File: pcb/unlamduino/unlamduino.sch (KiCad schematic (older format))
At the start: 37 parts, among them IC2 ATMEGA328-P, P3 CONN_01X08, U1 LM2576, U2 AP111733, Y2 16MHz

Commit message: Primera asignacion de encapsulados a las partes del circuito.
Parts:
- AD1: footprint (none) -> Pin_Headers:Pin_Header_Straight_1x06
- C1, C3: footprint (none) -> Capacitors_ThroughHole:C_Radial_D6.3_L11.2_P2.5
- C10, C2, C4, C5, C6, C7, C9: footprint (none) -> Capacitors_ThroughHole:C_Disc_D6_P5
- C20, C21: footprint (none) -> Capacitors_ThroughHole:C_Disc_D3_P2.5
- C8: footprint (none) -> Capacitors_ThroughHole:C_Radial_D7.5_L11.2_P2.5
- D2, D5, D6: footprint (none) -> Diodes_ThroughHole:Diode_DO-41_SOD81_Horizontal_RM10
- D4, DR1: footprint (none) -> LEDs:LED-5MM
- ICSP2: footprint (none) -> Pin_Headers:Pin_Header_Straight_2x03
- IOH1: footprint (none) -> Pin_Headers:Pin_Header_Straight_1x10
- IOL1, P3: footprint (none) -> Pin_Headers:Pin_Header_Straight_1x08
- JP1: footprint (none) -> Connect:BARREL_JACK
- L2: footprint (none) -> Resistors_ThroughHole:Resistor_Horizontal_RM10mm
- L3: footprint (none) -> Discret:CP36V
- PSerial1: footprint (none) -> Pin_Headers:Pin_Header_Straight_1x04
- PWR1: footprint (none) -> Connect:bornier2
- R1, R8, R9, RN1, RN2: footprint (none) -> Resistors_ThroughHole:Resistor_Horizontal_RM15mm
- RESET1: footprint (none) -> Buttons_Switches_ThroughHole:SW_PUSH_SMALL
- U1: footprint (none) -> TO_SOT_Packages_THT:Pentawatt_Neutral_Staggered_Verical_TO220-5-T05D
- Y2: footprint (none) -> Crystals:Crystal_HC51-U_Vertical
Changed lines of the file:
@@
 F 0 "IOL1" H 7400 5950 50  0000 C CNN
 F 1 "CONN_01X08" V 7500 5500 50  0001 C CNN
-F 2 "" H 7400 5500 60  0000 C CNN
+F 2 "Pin_Headers:Pin_Header_Straight_1x08" H 7400 5500 60  0001 C CNN
 F 3 "" H 7400 5500 60  0000 C CNN
 	1    7400 5500
@@
 F 0 "IOH1" H 8850 4550 50  0000 C CNN
 F 1 "CONN_01X10" V 8950 4000 50  0001 C CNN
-F 2 "" H 8850 4000 60  0000 C CNN
+F 2 "Pin_Headers:Pin_Header_Straight_1x10" H 8850 4000 60  0001 C CNN
 F 3 "" H 8850 4000 60  0000 C CNN
 	1    8850 4000
@@
 F 0 "ICSP2" H 10100 4850 50  0000 C CNN
 F 1 "CONN_02X03" H 10100 4450 50  0000 C CNN
-F 2 "" H 10100 3450 60  0000 C CNN
+F 2 "Pin_Headers:Pin_Header_Straight_2x03" H 10100 3450 60  0001 C CNN
 F 3 "" H 10100 3450 60  0000 C CNN
 	1    10100 4650
@@
 F 0 "C10" H 2750 4700 50  0000 L CNN
 F 1 "100nF" H 2750 4600 50  0000 L CNN
-F 2 "" H 2600 4600 60  0000 C CNN
+F 2 "Capacitors_ThroughHole:C_Disc_D6_P5" H 2600 4600 60  0001 C CNN
 F 3 "" H 2600 4600 60  0000 C CNN
 	1    2600 4600
@@
 F 0 "D4" H 7150 2650 50  0000 L CNN
 F 1 "Verde" H 7050 2470 50  0000 L CNN
-F 2 "" V 7200 2550 60  0000 C CNN
+F 2 "LEDs:LED-5MM" V 7200 2550 60  0001 C CNN
 F 3 "" V 7200 2550 60  0000 C CNN
 	1    7200 2550
@@
 F 0 "R8" V 4750 6400 50  0000 C CNN
 F 1 "1K" V 4850 6400 50  0000 C CNN
-F 2 "" V 4780 6400 50  0000 C CNN
+F 2 "Resistors_ThroughHole:Resistor_Horizontal_RM15mm" V 4780 6400 50  0001 C CNN
 F 3 "" H 4850 6400 50  0000 C CNN
 	1    4850 6400
@@
 F 0 "R9" V 4930 6500 50  0000 C CNN
 F 1 "1K" V 4850 6500 50  0000 C CNN
-F 2 "" V 4780 6500 50  0000 C CNN
+F 2 "Resistors_ThroughHole:Resistor_Horizontal_RM15mm" V 4780 6500 50  0001 C CNN
 F 3 "" H 4850 6500 50  0000 C CNN
 	1    4850 6500
@@
 F 0 "C7" H 2275 4100 50  0000 L CNN
 F 1 "100nF" H 2275 3900 50  0000 L CNN
-F 2 "" H 2288 3850 50  0000 C CNN
+F 2 "Capacitors_ThroughHole:C_Disc_D6_P5" H 2288 3850 50  0001 C CNN
 F 3 "" H 2250 4000 50  0000 C CNN
 	1    2250 4000
@@
 F 0 "C5" H 1975 4100 50  0000 L CNN
 F 1 "100nF" H 1975 3900 50  0000 L CNN
-F 2 "" H 1988 3850 50  0000 C CNN
+F 2 "Capacitors_ThroughHole:C_Disc_D6_P5" H 1988 3850 50  0001 C CNN
 F 3 "" H 1950 4000 50  0000 C CNN
 	1    1950 4000
@@
 F 0 "L2" V 2200 3900 50  0000 L CNN
 F 1 "L_Small" V 2200 3550 50  0000 L CNN
-F 2 "" H 2100 3850 50  0000 C CNN
+F 2 "Resistors_ThroughHole:Resistor_Horizontal_RM10mm" H 2100 3850 50  0001 C CNN
 F 3 "" H 2100 3850 50  0000 C CNN
 	1    2100 3850
@@
 F 0 "Y2" V 9550 5800 50  0000 C CNN
 F 1 "16MHz" V 9650 5800 50  0000 C CNN
-F 2 "" H 9850 5800 50  0000 C CNN
+F 2 "Crystals:Crystal_HC51-U_Vertical" H 9850 5800 50  0001 C CNN
 F 3 "" H 9850 5800 50  0000 C CNN
 	1    9850 5800
@@
 F 0 "C20" V 9950 5600 50  0000 L CNN
 F 1 "22pF" V 9850 5600 50  0000 L CNN
-F 2 "" H 10188 5500 50  0000 C CNN
+F 2 "Capacitors_ThroughHole:C_Disc_D3_P2.5" H 10188 5500 50  0001 C CNN
 F 3 "" H 10150 5650 50  0000 C CNN
 	1    10150 5650
@@
 F 0 "C21" V 10300 5900 50  0000 L CNN
 F 1 "22pF" V 10400 5900 50  0000 L CNN
-F 2 "" H 10188 5800 50  0000 C CNN
+F 2 "Capacitors_ThroughHole:C_Disc_D3_P2.5" H 10188 5800 50  0001 C CNN
 F 3 "" H 10150 5950 50  0000 C CNN
 	1    10150 5950
@@
 F 0 "RN1" V 1450 5800 50  0000 C CNN
 F 1 "10K" V 1550 5800 50  0000 C CNN
-F 2 "" V 1480 5800 50  0000 C CNN
+F 2 "Resistors_ThroughHole:Resistor_Horizontal_RM15mm" V 1480 5800 50  0001 C CNN
 F 3 "" H 1550 5800 50  0000 C CNN
 	1    1550 5800
@@
 F 0 "C6" H 1300 6550 50  0000 L CNN
 F 1 "100nF" H 1300 6650 50  0000 L CNN
-F 2 "" H 1588 6400 50  0000 C CNN
+F 2 "Capacitors_ThroughHole:C_Disc_D6_P5" H 1588 6400 50  0001 C CNN
 F 3 "" H 1550 6550 50  0000 C CNN
 	1    1550 6550
@@
 F 0 "RESET1" H 1950 6660 50  0000 C CNN
 F 1 "SW_PUSH" H 1800 6470 50  0000 C CNN
-F 2 "" H 1800 6550 50  0000 C CNN
+F 2 "Buttons_Switches_ThroughHole:SW_PUSH_SMALL" H 1800 6550 50  0001 C CNN
 F 3 "" H 1800 6550 50  0000 C CNN
 	1    1800 6550
@@
 F 0 "P3" H 10400 4000 50  0000 C CNN
 F 1 "CONN_01X08" V 10500 3450 50  0000 C CNN
-F 2 "" H 10400 3450 50  0000 C CNN
+F 2 "Pin_Headers:Pin_Header_Straight_1x08" H 10400 3450 50  0001 C CNN
 F 3 "" H 10400 3450 50  0000 C CNN
 	1    10400 3450
@@
 F 0 "D5" H 3250 2000 50  0000 C CNN
 F 1 "1N4007" H 3250 1800 50  0000 C CNN
-F 2 "" H 3250 1900 50  0000 C CNN
+F 2 "Diodes_ThroughHole:Diode_DO-41_SOD81_Horizontal_RM10" H 3250 1900 50  0001 C CNN
 F 3 "" H 3250 1900 50  0000 C CNN
 	1    3250 1900
@@
 F 0 "C2" H 3875 2400 50  0000 L CNN
 F 1 "100nF" H 3875 2200 50  0000 L CNN
-F 2 "" H 3888 2150 50  0000 C CNN
+F 2 "Capacitors_ThroughHole:C_Disc_D6_P5" H 3888 2150 50  0001 C CNN
 F 3 "" H 3850 2300 50  0000 C CNN
 	1    3850 2300
@@
 F 0 "C1" H 3575 2400 50  0000 L CNN
 F 1 "100uF 35V" H 3100 2150 50  0000 L CNN
-F 2 "" H 3550 2300 50  0000 C CNN
+F 2 "Capacitors_ThroughHole:C_Radial_D6.3_L11.2_P2.5" H 3550 2300 50  0001 C CNN
 F 3 "" H 3550 2300 50  0000 C CNN
 	1    3550 2300
@@
 F 0 "C4" H 6825 2400 50  0000 L CNN
 F 1 "100nF" H 6850 2200 50  0000 L CNN
-F 2 "" H 6838 2150 50  0000 C CNN
+F 2 "Capacitors_ThroughHole:C_Disc_D6_P5" H 6838 2150 50  0001 C CNN
 F 3 "" H 6800 2300 50  0000 C CNN
 	1    6800 2300
@@
 F 0 "C3" H 6525 2400 50  0000 L CNN
 F 1 "100uF 16v" H 6250 2150 50  0000 L CNN
-F 2 "" H 6500 2300 50  0000 C CNN
+F 2 "Capacitors_ThroughHole:C_Radial_D6.3_L11.2_P2.5" H 6500 2300 50  0001 C CNN
 F 3 "" H 6500 2300 50  0000 C CNN
 	1    6500 2300
@@
 F 0 "D6" H 5800 2400 50  0000 C CNN
 F 1 "1N5819" H 5800 2200 50  0000 C CNN
-F 2 "" H 5800 2300 50  0000 C CNN
+F 2 "Diodes_ThroughHole:Diode_DO-41_SOD81_Horizontal_RM10" H 5800 2300 50  0001 C CNN
 F 3 "" H 5800 2300 50  0000 C CNN
 	1    5800 2300
@@
 F 0 "L3" V 6000 1950 50  0000 L CNN
 F 1 "330uHy" V 5900 1850 50  0000 L CNN
-F 2 "" H 6050 2000 50  0000 C CNN
+F 2 "Discret:CP36V" H 6050 2000 50  0001 C CNN
 F 3 "" H 6050 2000 50  0000 C CNN
 	1    6050 2000
@@
 F 0 "U1" H 4300 2350 50  0000 C CNN
 F 1 "LM2576" H 4400 2250 50  0000 C CNN
-F 2 "" H 4800 1950 79  0001 C CNN
+F 2 "TO_SOT_Packages_THT:Pentawatt_Neutral_Staggered_Verical_TO220-5-T05D" H 4800 1950 79  0001 C CNN
 F 3 "" H 4800 1950 79  0001 C CNN
 	1    4800 1950
@@
 F 0 "R1" H 7100 2050 50  0000 C CNN
 F 1 "470" V 7200 2200 50  0000 C CNN
-F 2 "" V 7130 2200 50  0000 C CNN
+F 2 "Resistors_ThroughHole:Resistor_Horizontal_RM15mm" V 7130 2200 50  0001 C CNN
 F 3 "" H 7200 2200 50  0000 C CNN
 	1    7200 2200
@@
 F 0 "D2" H 1800 5950 50  0000 C CNN
 F 1 "1N4007" H 1800 5750 50  0000 C CNN
-F 2 "" H 1800 5850 50  0000 C CNN
+F 2 "Diodes_ThroughHole:Diode_DO-41_SOD81_Horizontal_RM10" H 1800 5850 50  0001 C CNN
 F 3 "" H 1800 5850 50  0000 C CNN
 	1    1800 5850
@@
 F 0 "AD1" H 7400 5000 50  0000 C CNN
 F 1 "CONN_01X06" V 7500 4650 50  0001 C CNN
-F 2 "" H 7400 4650 60  0000 C CNN
+F 2 "Pin_Headers:Pin_Header_Straight_1x06" H 7400 4650 60  0001 C CNN
 F 3 "" H 7400 4650 60  0000 C CNN
 	1    7400 4650
@@
 F 0 "RN2" H 7750 4200 50  0000 C CNN
 F 1 "1K" V 7850 4350 50  0000 C CNN
-F 2 "" V 7780 4350 50  0000 C CNN
+F 2 "Resistors_ThroughHole:Resistor_Horizontal_RM15mm" V 7780 4350 50  0001 C CNN
 F 3 "" H 7850 4350 50  0000 C CNN
 	1    7850 4350
@@
 F 0 "DR1" H 7800 4800 50  0000 L CNN
 F 1 "Rojo" H 7700 4620 50  0000 L CNN
-F 2 "" V 7850 4700 60  0000 C CNN
+F 2 "LEDs:LED-5MM" V 7850 4700 60  0001 C CNN
 F 3 "" V 7850 4700 60  0000 C CNN
 	1    7850 4700
@@
 F 0 "PWR1" H 1800 2100 50  0000 C CNN
 F 1 "CONN_01X02" V 1900 1950 50  0001 C CNN
-F 2 "" H 1800 1950 50  0000 C CNN
+F 2 "Connect:bornier2" H 1800 1950 50  0001 C CNN
 F 3 "" H 1800 1950 50  0000 C CNN
 	1    1800 1950
@@
 F 0 "PSerial1" H 3950 6700 50  0000 C CNN
 F 1 "CONN_01X04" V 4050 6450 50  0001 C CNN
-F 2 "" H 3950 6450 50  0000 C CNN
+F 2 "Pin_Headers:Pin_Header_Straight_1x04" H 3950 6450 50  0001 C CNN
 F 3 "" H 3950 6450 50  0000 C CNN
 	1    3950 6450
@@
 F 0 "JP1" H 1700 1250 50  0000 C CNN
 F 1 "JACK_2P" H 1900 1700 50  0000 C CNN
-F 2 "" H 2050 1450 50  0000 C CNN
+F 2 "Connect:BARREL_JACK" H 2050 1450 50  0001 C CNN
 F 3 "" H 2050 1450 50  0000 C CNN
 	1    2050 1450
@@
 F 0 "C9" H 8375 2400 50  0000 L CNN
 F 1 "100nF" H 8400 2200 50  0000 L CNN
-F 2 "" H 8388 2150 50  0000 C CNN
+F 2 "Capacitors_ThroughHole:C_Disc_D6_P5" H 8388 2150 50  0001 C CNN
 F 3 "" H 8350 2300 50  0000 C CNN
 	1    8350 2300
@@
 F 0 "C8" H 8075 2400 50  0000 L CNN
 F 1 "100uF 16v" H 7800 2150 50  0000 L CNN
-F 2 "" H 8050 2300 50  0000 C CNN
+F 2 "Capacitors_ThroughHole:C_Radial_D7.5_L11.2_P2.5" H 8050 2300 50  0001 C CNN
 F 3 "" H 8050 2300 50  0000 C CNN
 	1    8050 2300

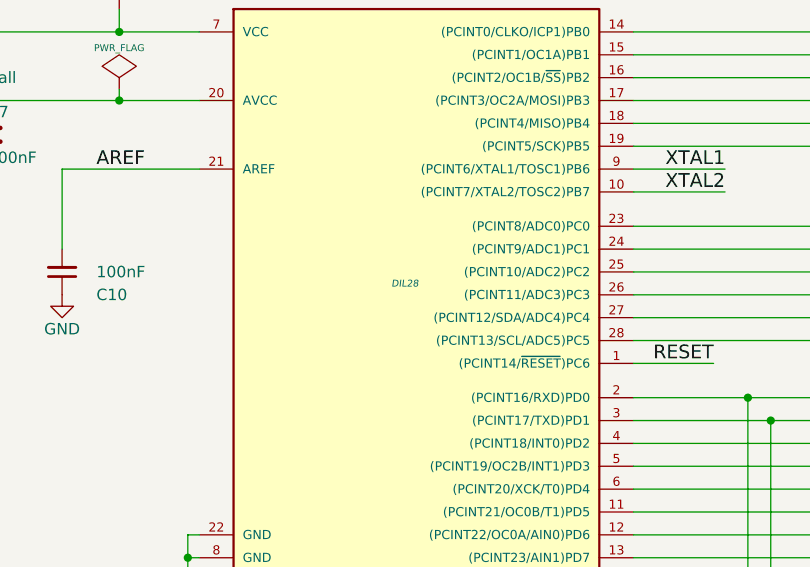
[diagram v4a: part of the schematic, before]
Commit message: Preliminar de posición de componentes en la placa.
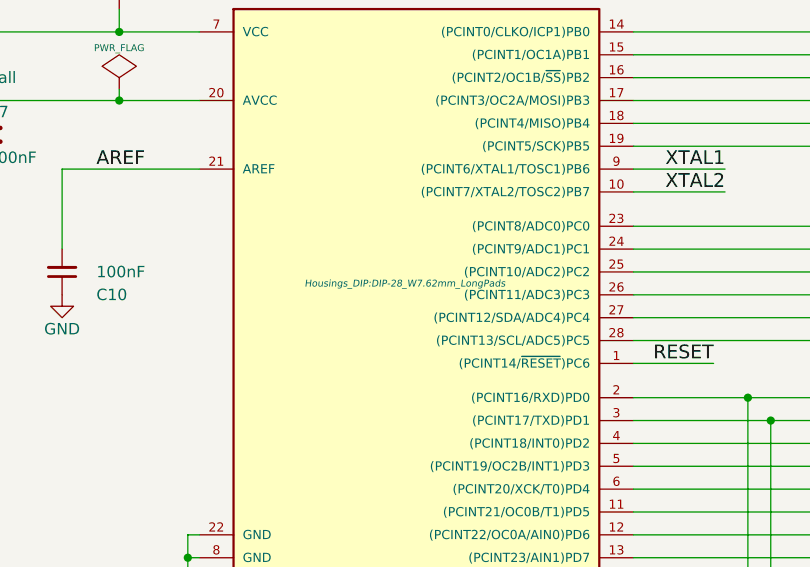
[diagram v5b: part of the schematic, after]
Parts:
- IC2: footprint DIL28 -> Housings_DIP:DIP-28_W7.62mm_LongPads
- L3: footprint Discret:CP36V -> Choke_Toroid_ThroughHole:Choke_Toroid_horizontal_Diameter4-5mm_Amidon-T16
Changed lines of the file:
@@
 F 0 "IC2" H 3350 5900 40  0000 L BNN
 F 1 "ATMEGA328-P" H 4500 3250 40  0000 L BNN
-F 2 "DIL28" H 4100 4650 30  0000 C CIN
+F 2 "Housings_DIP:DIP-28_W7.62mm_LongPads" H 4100 4650 30  0000 C CIN
 F 3 "" H 4100 4650 60  0000 C CNN
 	1    4100 4650
@@
 F 0 "L3" V 6000 1950 50  0000 L CNN
 F 1 "330uHy" V 5900 1850 50  0000 L CNN
-F 2 "Discret:CP36V" H 6050 2000 50  0001 C CNN
+F 2 "Choke_Toroid_ThroughHole:Choke_Toroid_horizontal_Diameter4-5mm_Amidon-T16" H 6050 2000 50  0001 C CNN
 F 3 "" H 6050 2000 50  0000 C CNN
 	1    6050 2000

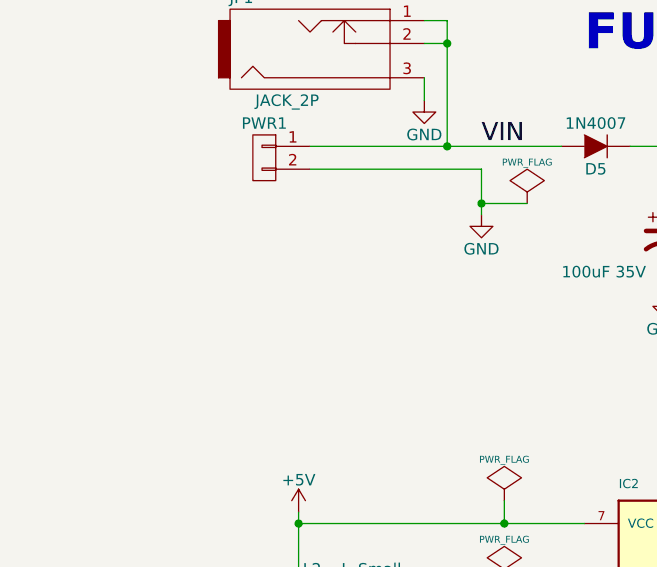
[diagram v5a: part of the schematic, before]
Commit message: Agujeros de fijación
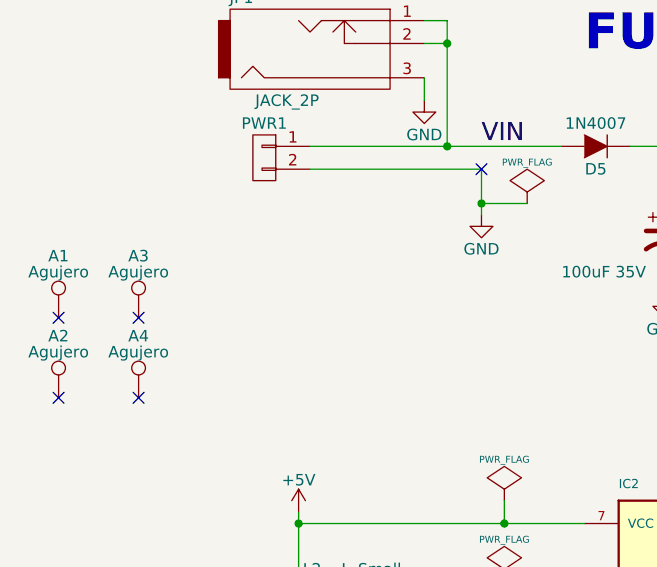
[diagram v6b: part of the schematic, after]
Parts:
- added A1, A2, A3, A4: Agujero, Mounting_Holes:MountingHole_3.2mm_M3_DIN965_Pad, symbol TEST_1P
- C10, C2, C4, C5, C6, C7, C9: footprint Capacitors_ThroughHole:C_Disc_D6_P5 -> Capacitors_ThroughHole:C_Disc_D3_P2.5
- C8: footprint Capacitors_ThroughHole:C_Radial_D7.5_L11.2_P2.5 -> Capacitors_ThroughHole:C_Radial_D6.3_L11.2_P2.5
- D2, D5, D6: footprint Diodes_ThroughHole:Diode_DO-41_SOD81_Horizontal_RM10 -> Diodes_ThroughHole:Diode_DO-35_SOD27_Horizontal_RM10
- R1, R8, R9, RN1, RN2: footprint Resistors_ThroughHole:Resistor_Horizontal_RM15mm -> Resistors_ThroughHole:Resistor_Horizontal_RM7mm
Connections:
- no-connect marks 1 -> 6
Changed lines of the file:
@@
 EESchema Schematic File Version 2
-LIBS:power
+LIBS:conn
 LIBS:unlamduino-cache
 EELAYER 25 0
@@
 F 0 "C10" H 2750 4700 50  0000 L CNN
 F 1 "100nF" H 2750 4600 50  0000 L CNN
-F 2 "Capacitors_ThroughHole:C_Disc_D6_P5" H 2600 4600 60  0001 C CNN
+F 2 "Capacitors_ThroughHole:C_Disc_D3_P2.5" H 2600 4600 60  0001 C CNN
 F 3 "" H 2600 4600 60  0000 C CNN
 	1    2600 4600
@@
 F 0 "R8" V 4750 6400 50  0000 C CNN
 F 1 "1K" V 4850 6400 50  0000 C CNN
-F 2 "Resistors_ThroughHole:Resistor_Horizontal_RM15mm" V 4780 6400 50  0001 C CNN
+F 2 "Resistors_ThroughHole:Resistor_Horizontal_RM7mm" V 4780 6400 50  0001 C CNN
 F 3 "" H 4850 6400 50  0000 C CNN
 	1    4850 6400
@@
 F 0 "R9" V 4930 6500 50  0000 C CNN
 F 1 "1K" V 4850 6500 50  0000 C CNN
-F 2 "Resistors_ThroughHole:Resistor_Horizontal_RM15mm" V 4780 6500 50  0001 C CNN
+F 2 "Resistors_ThroughHole:Resistor_Horizontal_RM7mm" V 4780 6500 50  0001 C CNN
 F 3 "" H 4850 6500 50  0000 C CNN
 	1    4850 6500
@@
 F 0 "C7" H 2275 4100 50  0000 L CNN
 F 1 "100nF" H 2275 3900 50  0000 L CNN
-F 2 "Capacitors_ThroughHole:C_Disc_D6_P5" H 2288 3850 50  0001 C CNN
+F 2 "Capacitors_ThroughHole:C_Disc_D3_P2.5" H 2288 3850 50  0001 C CNN
 F 3 "" H 2250 4000 50  0000 C CNN
 	1    2250 4000
@@
 F 0 "C5" H 1975 4100 50  0000 L CNN
 F 1 "100nF" H 1975 3900 50  0000 L CNN
-F 2 "Capacitors_ThroughHole:C_Disc_D6_P5" H 1988 3850 50  0001 C CNN
+F 2 "Capacitors_ThroughHole:C_Disc_D3_P2.5" H 1988 3850 50  0001 C CNN
 F 3 "" H 1950 4000 50  0000 C CNN
 	1    1950 4000
@@
 F 0 "RN1" V 1450 5800 50  0000 C CNN
 F 1 "10K" V 1550 5800 50  0000 C CNN
-F 2 "Resistors_ThroughHole:Resistor_Horizontal_RM15mm" V 1480 5800 50  0001 C CNN
+F 2 "Resistors_ThroughHole:Resistor_Horizontal_RM7mm" V 1480 5800 50  0001 C CNN
 F 3 "" H 1550 5800 50  0000 C CNN
 	1    1550 5800
@@
 F 0 "C6" H 1300 6550 50  0000 L CNN
 F 1 "100nF" H 1300 6650 50  0000 L CNN
-F 2 "Capacitors_ThroughHole:C_Disc_D6_P5" H 1588 6400 50  0001 C CNN
+F 2 "Capacitors_ThroughHole:C_Disc_D3_P2.5" H 1588 6400 50  0001 C CNN
 F 3 "" H 1550 6550 50  0000 C CNN
 	1    1550 6550
@@
 F 0 "D5" H 3250 2000 50  0000 C CNN
 F 1 "1N4007" H 3250 1800 50  0000 C CNN
-F 2 "Diodes_ThroughHole:Diode_DO-41_SOD81_Horizontal_RM10" H 3250 1900 50  0001 C CNN
+F 2 "Diodes_ThroughHole:Diode_DO-35_SOD27_Horizontal_RM10" H 3250 1900 50  0001 C CNN
 F 3 "" H 3250 1900 50  0000 C CNN
 	1    3250 1900
@@
 F 0 "C2" H 3875 2400 50  0000 L CNN
 F 1 "100nF" H 3875 2200 50  0000 L CNN
-F 2 "Capacitors_ThroughHole:C_Disc_D6_P5" H 3888 2150 50  0001 C CNN
+F 2 "Capacitors_ThroughHole:C_Disc_D3_P2.5" H 3888 2150 50  0001 C CNN
 F 3 "" H 3850 2300 50  0000 C CNN
 	1    3850 2300
@@
 F 0 "C4" H 6825 2400 50  0000 L CNN
 F 1 "100nF" H 6850 2200 50  0000 L CNN
-F 2 "Capacitors_ThroughHole:C_Disc_D6_P5" H 6838 2150 50  0001 C CNN
+F 2 "Capacitors_ThroughHole:C_Disc_D3_P2.5" H 6838 2150 50  0001 C CNN
 F 3 "" H 6800 2300 50  0000 C CNN
 	1    6800 2300
@@
 F 0 "D6" H 5800 2400 50  0000 C CNN
 F 1 "1N5819" H 5800 2200 50  0000 C CNN
-F 2 "Diodes_ThroughHole:Diode_DO-41_SOD81_Horizontal_RM10" H 5800 2300 50  0001 C CNN
+F 2 "Diodes_ThroughHole:Diode_DO-35_SOD27_Horizontal_RM10" H 5800 2300 50  0001 C CNN
 F 3 "" H 5800 2300 50  0000 C CNN
 	1    5800 2300
@@
 F 0 "R1" H 7100 2050 50  0000 C CNN
 F 1 "470" V 7200 2200 50  0000 C CNN
-F 2 "Resistors_ThroughHole:Resistor_Horizontal_RM15mm" V 7130 2200 50  0001 C CNN
+F 2 "Resistors_ThroughHole:Resistor_Horizontal_RM7mm" V 7130 2200 50  0001 C CNN
 F 3 "" H 7200 2200 50  0000 C CNN
 	1    7200 2200
@@
 F 0 "D2" H 1800 5950 50  0000 C CNN
 F 1 "1N4007" H 1800 5750 50  0000 C CNN
-F 2 "Diodes_ThroughHole:Diode_DO-41_SOD81_Horizontal_RM10" H 1800 5850 50  0001 C CNN
+F 2 "Diodes_ThroughHole:Diode_DO-35_SOD27_Horizontal_RM10" H 1800 5850 50  0001 C CNN
 F 3 "" H 1800 5850 50  0000 C CNN
 	1    1800 5850
@@
 F 0 "RN2" H 7750 4200 50  0000 C CNN
 F 1 "1K" V 7850 4350 50  0000 C CNN
-F 2 "Resistors_ThroughHole:Resistor_Horizontal_RM15mm" V 7780 4350 50  0001 C CNN
+F 2 "Resistors_ThroughHole:Resistor_Horizontal_RM7mm" V 7780 4350 50  0001 C CNN
 F 3 "" H 7850 4350 50  0000 C CNN
 	1    7850 4350
@@
 F 0 "C9" H 8375 2400 50  0000 L CNN
 F 1 "100nF" H 8400 2200 50  0000 L CNN
-F 2 "Capacitors_ThroughHole:C_Disc_D6_P5" H 8388 2150 50  0001 C CNN
+F 2 "Capacitors_ThroughHole:C_Disc_D3_P2.5" H 8388 2150 50  0001 C CNN
 F 3 "" H 8350 2300 50  0000 C CNN
 	1    8350 2300
@@
 F 0 "C8" H 8075 2400 50  0000 L CNN
 F 1 "100uF 16v" H 7800 2150 50  0000 L CNN
-F 2 "Capacitors_ThroughHole:C_Radial_D7.5_L11.2_P2.5" H 8050 2300 50  0001 C CNN
+F 2 "Capacitors_ThroughHole:C_Radial_D6.3_L11.2_P2.5" H 8050 2300 50  0001 C CNN
 F 3 "" H 8050 2300 50  0000 C CNN
 	1    8050 2300
@@
 	1    0    0    -1
 $EndComp
+$Comp
+L TEST_1P A1
+U 1 1 58080CA5
+P 900 2650
+F 0 "A1" H 900 2920 50  0000 C CNN
+F 1 "Agujero" H 900 2850 50  0000 C CNN
+F 2 "Mounting_Holes:MountingHole_3.2mm_M3_DIN965_Pad" H 1100 2650 50  0001 C CNN
+F 3 "" H 1100 2650 50  0000 C CNN
+	1    900  2650
+	1    0    0    -1
+$EndComp
+NoConn ~ 900  2650
+NoConn ~ 2750 2000
+$Comp
+L TEST_1P A3
+U 1 1 58080F61
+P 1250 2650
+F 0 "A3" H 1250 2920 50  0000 C CNN
+F 1 "Agujero" H 1250 2850 50  0000 C CNN
+F 2 "Mounting_Holes:MountingHole_3.2mm_M3_DIN965_Pad" H 1450 2650 50  0001 C CNN
+F 3 "" H 1450 2650 50  0000 C CNN
+	1    1250 2650
+	1    0    0    -1
+$EndComp
+NoConn ~ 1250 2650
+$Comp
+L TEST_1P A2
+U 1 1 58080FE0
+P 900 3000
+F 0 "A2" H 900 3270 50  0000 C CNN
+F 1 "Agujero" H 900 3200 50  0000 C CNN
+F 2 "Mounting_Holes:MountingHole_3.2mm_M3_DIN965_Pad" H 1100 3000 50  0001 C CNN
+F 3 "" H 1100 3000 50  0000 C CNN
+	1    900  3000
+	1    0    0    -1
+$EndComp
+NoConn ~ 900  3000
+$Comp
+L TEST_1P A4
+U 1 1 58080FE7
+P 1250 3000
+F 0 "A4" H 1250 3270 50  0000 C CNN
+F 1 "Agujero" H 1250 3200 50  0000 C CNN
+F 2 "Mounting_Holes:MountingHole_3.2mm_M3_DIN965_Pad" H 1450 3000 50  0001 C CNN
+F 3 "" H 1450 3000 50  0000 C CNN
+	1    1250 3000
+	1    0    0    -1
+$EndComp
+NoConn ~ 1250 3000
 $EndSCHEMATC

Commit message: Corrección agujeros de montaje.
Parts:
- A1, A2, A3, A4: footprint Mounting_Holes:MountingHole_3.2mm_M3_DIN965_Pad -> Mounting_Holes:MountingHole_3.2mm_M3
- Y2: footprint Crystals:Crystal_HC51-U_Vertical -> Crystals:Crystal_HC50-U_Vertical
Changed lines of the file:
@@
 F 0 "Y2" V 9550 5800 50  0000 C CNN
 F 1 "16MHz" V 9650 5800 50  0000 C CNN
-F 2 "Crystals:Crystal_HC51-U_Vertical" H 9850 5800 50  0001 C CNN
+F 2 "Crystals:Crystal_HC50-U_Vertical" H 9850 5800 50  0001 C CNN
 F 3 "" H 9850 5800 50  0000 C CNN
 	1    9850 5800
@@
 F 0 "A1" H 900 2920 50  0000 C CNN
 F 1 "Agujero" H 900 2850 50  0000 C CNN
-F 2 "Mounting_Holes:MountingHole_3.2mm_M3_DIN965_Pad" H 1100 2650 50  0001 C CNN
+F 2 "Mounting_Holes:MountingHole_3.2mm_M3" H 1100 2650 50  0001 C CNN
 F 3 "" H 1100 2650 50  0000 C CNN
 	1    900  2650
@@
 F 0 "A3" H 1250 2920 50  0000 C CNN
 F 1 "Agujero" H 1250 2850 50  0000 C CNN
-F 2 "Mounting_Holes:MountingHole_3.2mm_M3_DIN965_Pad" H 1450 2650 50  0001 C CNN
+F 2 "Mounting_Holes:MountingHole_3.2mm_M3" H 1450 2650 50  0001 C CNN
 F 3 "" H 1450 2650 50  0000 C CNN
 	1    1250 2650
@@
 F 0 "A2" H 900 3270 50  0000 C CNN
 F 1 "Agujero" H 900 3200 50  0000 C CNN
-F 2 "Mounting_Holes:MountingHole_3.2mm_M3_DIN965_Pad" H 1100 3000 50  0001 C CNN
+F 2 "Mounting_Holes:MountingHole_3.2mm_M3" H 1100 3000 50  0001 C CNN
 F 3 "" H 1100 3000 50  0000 C CNN
 	1    900  3000
@@
 F 0 "A4" H 1250 3270 50  0000 C CNN
 F 1 "Agujero" H 1250 3200 50  0000 C CNN
-F 2 "Mounting_Holes:MountingHole_3.2mm_M3_DIN965_Pad" H 1450 3000 50  0001 C CNN
+F 2 "Mounting_Holes:MountingHole_3.2mm_M3" H 1450 3000 50  0001 C CNN
 F 3 "" H 1450 3000 50  0000 C CNN
 	1    1250 3000
